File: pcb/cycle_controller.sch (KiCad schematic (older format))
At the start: 0 parts

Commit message: started stm
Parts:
- added C? (x6): 0.1uF, 10V, RespiraWorks_std:C_0603_1608Metric, symbol Device:C
- added C?: 4.7uF, 10V, RespiraWorks_std:C_0603_1608Metric, symbol Device:C
- added C?: 1uF, 10V, RespiraWorks_std:C_0603_1608Metric, symbol Device:C
- added C? (x2): 20pF, RespiraWorks_std:C_0603_1608Metric, symbol Device:C
- added JP? (x2): Jumper, symbol Device:Jumper
- added R? (x2): 0, RespiraWorks_std:R_0603_1608Metric, symbol Device:R
- added R?: 10K, RespiraWorks_std:R_0603_1608Metric, symbol Device:R
- added SW?: SW_Push, symbol Switch:SW_Push
- added U?: STM32L496RGTx, Package_QFP:LQFP-64_10x10mm_P0.5mm, symbol MCU_ST_STM32L4:STM32L496RGTx
- added Y?: 8MHz(16pF), symbol Device:Crystal
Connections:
- new net: JP?.2, R?.1, U?.3 (PC14)
- new net: R?.1, U?.4 (PC15)
- new net: C?.1, SW?.1, U?.7 (NRST)
- new net: C?.2, R?.2, Y?.1
- new net: C?.2, R?.2, Y?.2
- new net +3.3V_Ctrl: C?.1, C?.1, C?.1, C?.1, C?.1, U?.1 (VBAT), U?.19 (VDD), U?.32 (VDD), U?.48 (VDDUSB), U?.64 (VDD)
- new net BOOT0: R?.2, U?.60 (PH3)
- new net CC-LED-G: U?.37 (PC6)
- new net CC-LED-R: U?.39 (PC8)
- new net CC-LED-Y: U?.40 (PC9)
- new net GND: C?.1, C?.1, C?.2, C?.2, C?.2, C?.2, C?.2, C?.2, C?.2, C?.2, JP?.1, R?.1, SW?.2, U?.18 (VSS), U?.31 (VSS), U?.47 (VSS), U?.63 (VSS)
- new net GNDA: JP?.2, U?.12 (VSSA)
- new net TCK: U?.49 (PA14)
- new net TDI: U?.50 (PA15)
- new net TDO: U?.55 (PB3)
- new net TMS: U?.46 (PA13)
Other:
- note added: "Check Boot0 pin"
- note added: "VDD pins"
- note added: "VDDA pins"
- note added: "Where is AVDD coming from? Power Conn for that as well?"

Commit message: stm continued
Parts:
- removed C? (x2): 20pF, RespiraWorks_std:C_0603_1608Metric, symbol Device:C
- removed JP?: Jumper, symbol Device:Jumper
- removed R? (x2): 0, RespiraWorks_std:R_0603_1608Metric, symbol Device:R
- removed Y?: 8MHz(16pF), symbol Device:Crystal
- added C? (x2): 20pF, RespiraWorks_std:C_0603_1608Metric, symbol Device:C
- added C? (x2): 6.8pF, RespiraWorks_std:C_0603_1608Metric, symbol Device:C
- added C?: 0.1uF, 10V, RespiraWorks_std:C_0603_1608Metric, symbol Device:C
- added JP? (x2): Jumper, symbol Device:Jumper
- added R? (x4): 0, RespiraWorks_std:R_0603_1608Metric, symbol Device:R
- added R?: 4.7K, RespiraWorks_std:R_0603_1608Metric, symbol Device:R
- added R?: 100, RespiraWorks_std:R_0603_1608Metric, symbol Device:R
- added SW?: SW_Push, symbol Switch:SW_Push
- added Y?: 8MHz(16pF), symbol Device:Crystal
- added Y?: ABS25-32.768KHZ-6-T, symbol Device:Crystal_GND23
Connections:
- net +3.3V_Ctrl: now also R?.2
- net GND: now also C?.1, C?.1, C?.2, C?.2, R?.2, SW?.2
- net MIXING-TANK-PRESSURE-OUT: now reaches U?.10 (PC2)
- net OXYGEN-PRESSURE-OUT: now reaches U?.11 (PC3)
- net TP-100-TEMP-SENSOR: now reaches U?.14 (PA0)
- net INH-FLOW-OUT: now reaches U?.15 (PA1)
- net USART-TX-STLINK: now reaches U?.16 (PA2)
- net USART-RX-STLINK: now reaches U?.17 (PA3)
- net at U?.2 (PC13): now also JP?.2
- net USD-nCS: now reaches U?.20 (PA4)
- net USD-SCLK: now reaches U?.21 (PA5)
- net USD-MISO: now reaches U?.22 (PA6)
- net USD-MOSI: now reaches U?.23 (PA7)
- net VIN-SENSE-OUT: now reaches U?.24 (PC4)
- net POWER-SWITCH-OVER: now reaches U?.25 (PC5)
- net SOLENOID-CTRL: now reaches U?.26 (PB0)
- net HEATER-CTRL: now reaches U?.27 (PB1)
- net BLOWER-CTRL: now reaches U?.28 (PB2)
- net at U?.3 (PC14): now also R?.1
- net USD-DETECT: now reaches U?.38 (PC7)
- net at U?.4 (PC15): now also R?.1
- net EXH-FLOW-OUT: now reaches U?.41 (PA8)
- net USART-TX: now reaches U?.42 (PA9)
- net USART-RX: now reaches U?.43 (PA10)
- net USART-CTS: now reaches U?.44 (PA11)
- net USART-RTS: now reaches U?.45 (PA12)
- net at U?.5 (PH0): now also JP?.2, R?.1
- net SWO: now reaches U?.51 (PC10)
- net OXY-FLOW-OUT: now reaches U?.56 (PB4)
- net at U?.6 (PH1): now also R?.1
- net CC-SCL: now reaches U?.61 (PB8)
- net CC-SDA: now reaches U?.62 (PB9)
- net OXYGEN-SENSOR: now reaches U?.8 (PC0)
- net PATIENT-PRESSURE-OUT: now reaches U?.9 (PC1)
- new net: C?.2, R?.2, Y?.1
- new net: C?.2, R?.2, Y?.2
- new net: C?.1, R?.2, Y?.1
- new net: C?.1, R?.2, Y?.4
- new net: C?.1, JP?.1, R?.1, SW?.1
- new net: C?.2, R?.1
- no-connect marks 0 -> 2
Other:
- note added: "Add fets for these here?"
- note added: "Add inputs from arduino connector?"
- note added: "Note: some pinouts changed, inform sw"
- moved on the sheet: R?

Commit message: most up to date
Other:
- note added: "Add VDD regulators or are those already somewhere"
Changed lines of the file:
@@
 Wire Wire Line
 	6700 4200 6400 4200
+Text Notes 2500 950  0    50   ~ 0
+Add VDD regulators or are those already somewhere
 $EndSCHEMATC

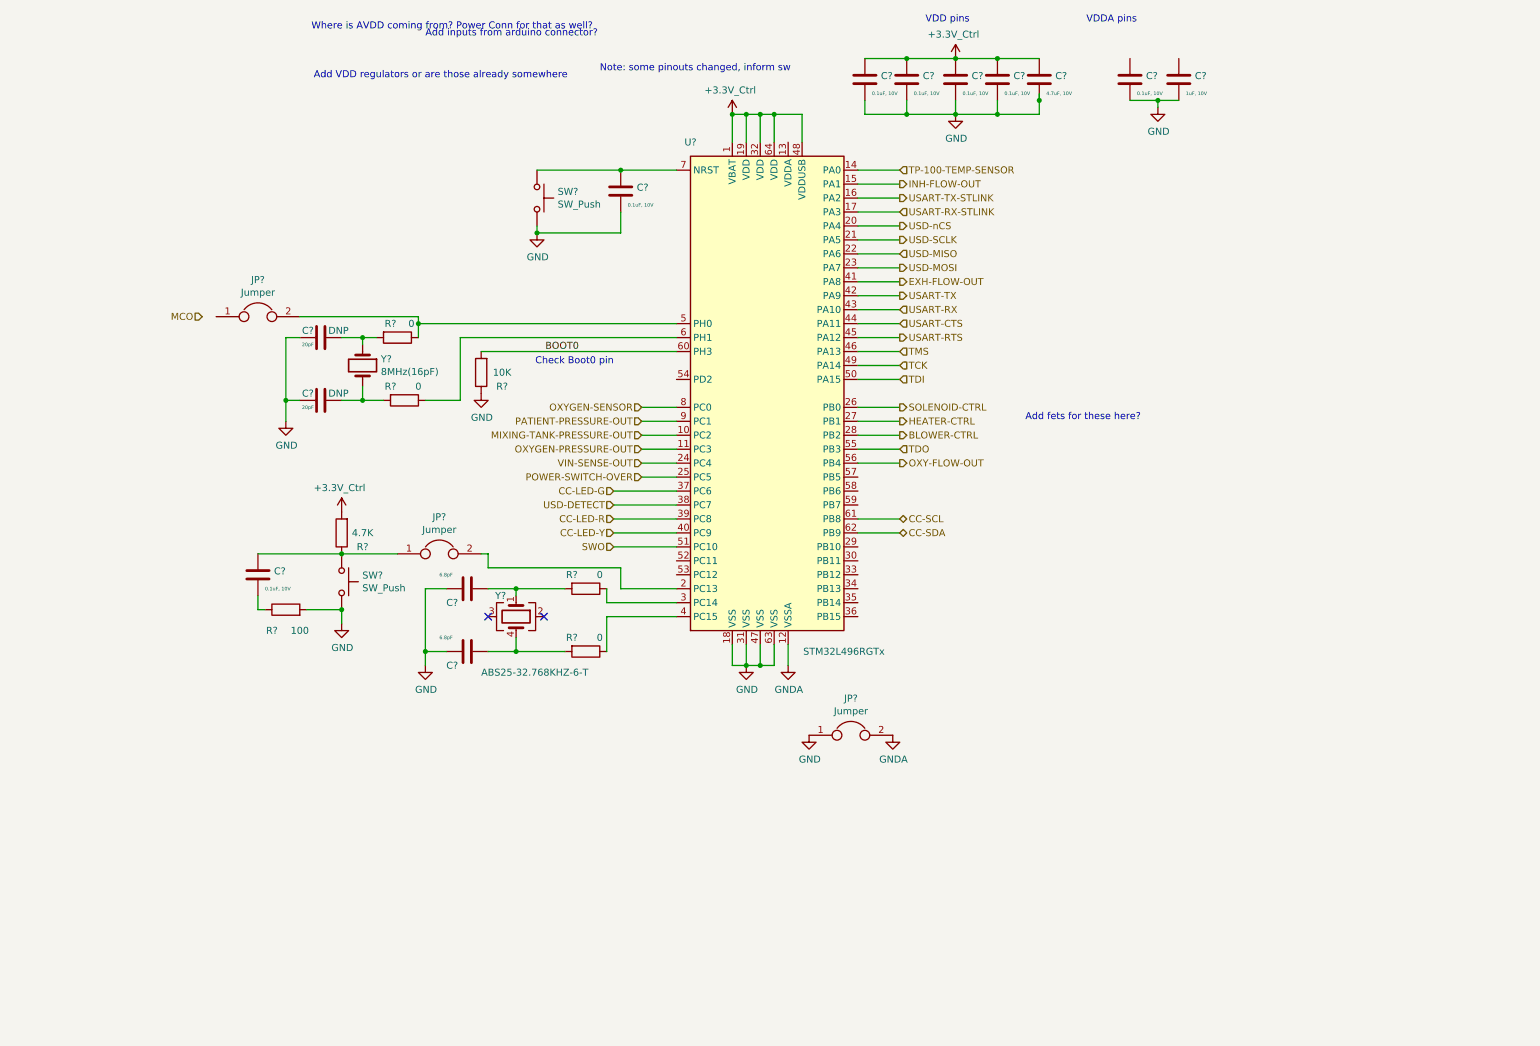
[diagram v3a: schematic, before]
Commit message: updated cycle controller
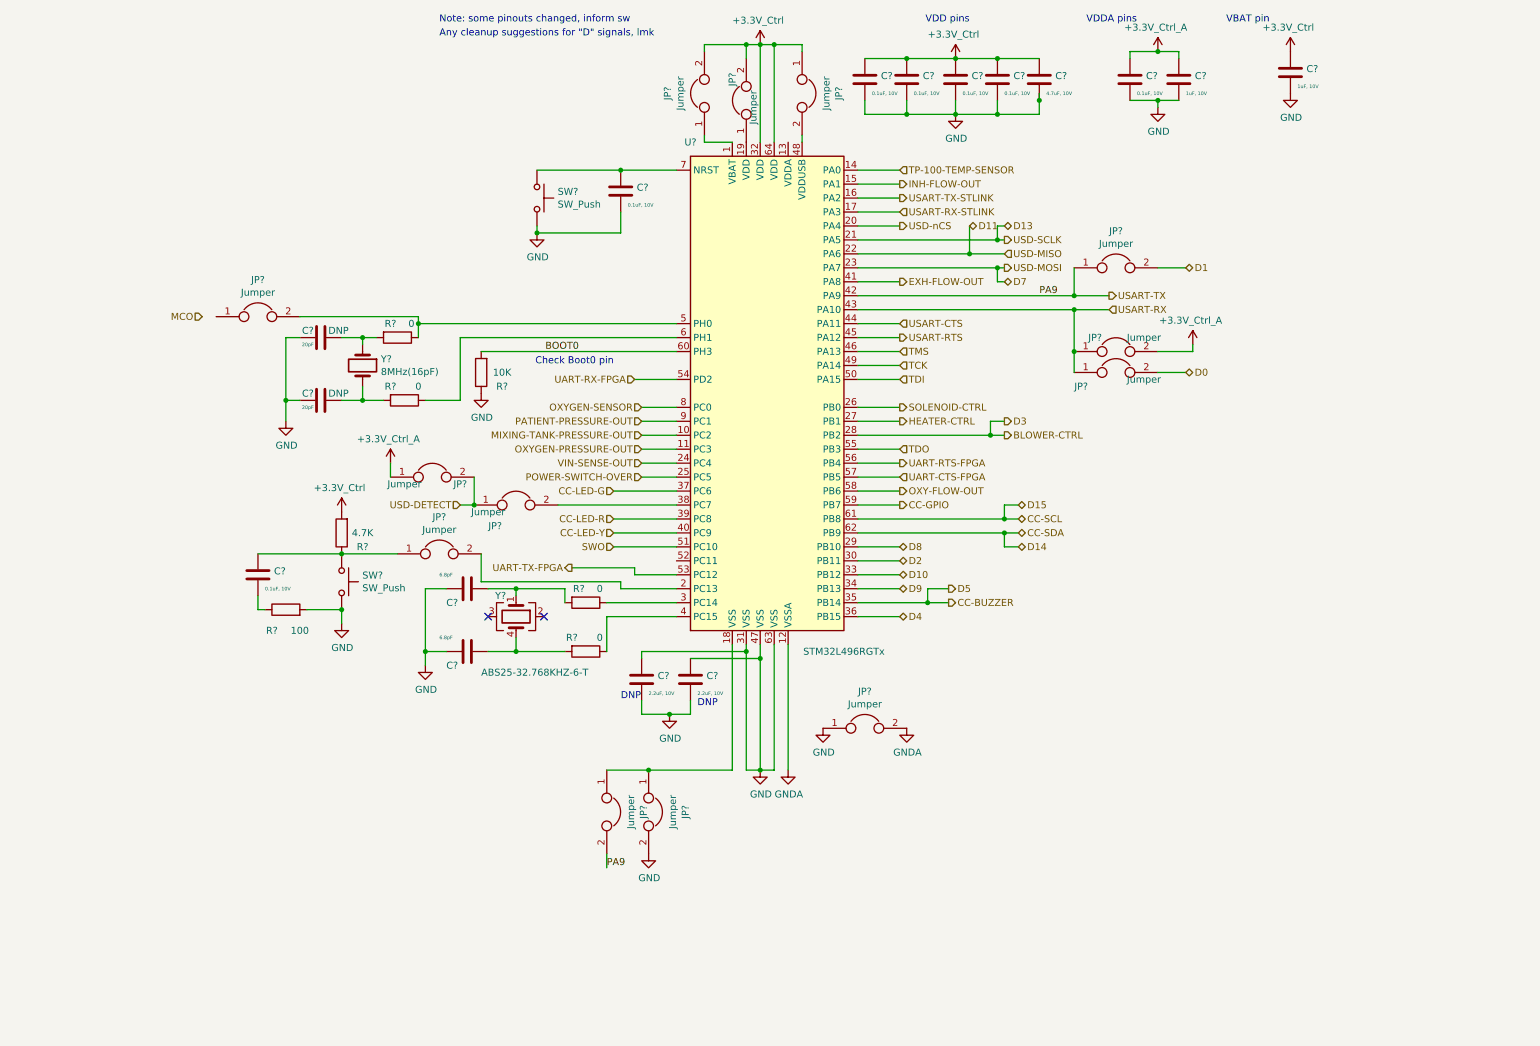
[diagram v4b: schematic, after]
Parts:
- added C?: 1uF, 10V, RespiraWorks_std:C_0603_1608Metric, symbol Device:C
- added C? (x2): 2.2uF, 10V, RespiraWorks_std:C_0603_1608Metric, symbol Device:C
- added JP? (x10): Jumper, symbol Device:Jumper
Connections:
- net +3.3V_Ctrl: now also C?.1, JP?.1, JP?.2, JP?.2; no longer U?.1 (VBAT), U?.19 (VDD), U?.48 (VDDUSB)
- net GND: now also C?.1, C?.1, C?.2, C?.2, C?.2, JP?.2; no longer U?.18 (VSS)
- net OXY-FLOW-OUT: now also U?.58 (PB6); no longer U?.56 (PB4)
- net USART-RX: now also JP?.1, JP?.1
- net USART-TX: now also JP?.1, JP?.2
- net USD-DETECT: now also JP?.1, JP?.2; no longer U?.38 (PC7)
- net D8: now reaches U?.29 (PB10)
- net D2: now reaches U?.30 (PB11)
- net D10: now reaches U?.33 (PB12)
- net D9: now reaches U?.34 (PB13)
- net CC-BUZZER: now reaches U?.35 (PB14)
- net D4: now reaches U?.36 (PB15)
- net UART-TX-FPGA: now reaches U?.53 (PC12)
- net UART-RX-FPGA: now reaches U?.54 (PD2)
- net UART-CTS-FPGA: now reaches U?.57 (PB5)
- net CC-GPIO: now reaches U?.59 (PB7)
- net +3.3V_Ctrl_A: now reaches C?.1
- net +3.3V_Ctrl_A: now also C?.1, JP?.1, JP?.2
- net USD-MISO renamed D11
- net USD-MOSI renamed D7
- net USD-SCLK renamed D13
- new net: JP?.1, U?.1 (VBAT)
- new net: JP?.1, JP?.1, U?.18 (VSS)
- new net: JP?.1, U?.19 (VDD)
- new net: JP?.2, U?.38 (PC7)
- new net: JP?.2, U?.48 (VDDUSB)
- new net D0: JP?.2
- new net D1: JP?.2
- new net UART-RTS-FPGA: U?.56 (PB4)
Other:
- note added: "Any cleanup suggestions for "D" signals, lmk"
- note added: "DNP"
- note added: "VBAT pin"
- note removed: "Add VDD regulators or are those already somewhere"
- note removed: "Add fets for these here?"
- note removed: "Add inputs from arduino connector?"
- note removed: "Where is AVDD coming from? Power Conn for that as well?"
- moved on the sheet: JP?, R?

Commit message: some cycle controller updates- more to come shortly
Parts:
- removed JP? (x10): Jumper, symbol Device:Jumper
- added C?: 1uF/10V, symbol Device:C
- added C?: 0.1uF/16V, symbol Device:C
- added C?: 1uF, 10V, RespiraWorks_std:C_0603_1608Metric, symbol Device:C
- added J?: 503182-1852, RespiraWorks:5031821852, symbol RespiraWorks:503182-1852
- added R? (x3): 10K, RespiraWorks_std:R_0603_1608Metric, symbol Device:R
- C? (x2), Y?: DNP (none) -> DNP
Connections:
- net USART-RX is gone; now on net D0: U?.43 (PA10)
- net USART-TX is gone; now on net D1: U?.42 (PA9)
- net +3.3V_Ctrl: now also U?.19 (VDD), U?.48 (VDDUSB), C?.1, C?.1, J?.4 (VDD), R?.1
- net +3.3V_Ctrl_A: now also U?.13 (VDDA), R?.1, R?.1
- net D0: now also R?.2
- net D11: now also J?.7 (DAT0)
- net D13: now also J?.5 (CLK)
- net D7: now also J?.3 (CMD)
- net GND: now also U?.18 (VSS), C?.2, C?.2, C?.2, J?.6 (VSS), J?.9 (Shield)
- net +BATT: now reaches JP?.1, U?.1 (VBAT)
- net +BATT: now also C?.1
- net USD-Detect: now reaches U?.38 (PC7)
- net USD-Detect: now also J?.Detect (DT), R?.2, R?.2
- net TP-100-TEMP-SENSOR: no longer names the net of U?.14 (PA0)
- new net USD-CS: J?.2 (CD/DAT3)
- no-connect marks 2 -> 6
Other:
- note added: "Double Check sw/dt footprint"
- note added: "Had trouble copying symbol to move VDDA to outside"
- note added: "Match name of power port for VDDA with the one from edwin's branch!"
- note added: "MicroSD Card Connector"
- note removed: "Any cleanup suggestions for "D" signals, lmk"
